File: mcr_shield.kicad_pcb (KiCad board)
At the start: 2 copper layers, 120 x 100 mm, 15 parts, among them J2 MCR_P1_Controls, J3 MCR_System_Coin, J4 MCR_Opt_X_Dial, J5 MCR_P2_Controls, SW1 Game_Selector, SW2 Cabinet_Options, U1 Buck_Regulator, U2 Optocoupler_P1, U3 Optocoupler_Sys, U4 Sync_Buffer, U5 Audio_Amplifier

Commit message: Add and route R2R DAC resistors (R1-R9) to KiCad PCB file
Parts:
- added R1: 3.9k_Red_LSB, R_Axial_DIN0207_L6.3mm_D2.5mm_P7.62mm_Horizontal, F.Cu at (40.0, 30.0)
- added R2: 2.0k_Red_Mid, R_Axial_DIN0207_L6.3mm_D2.5mm_P7.62mm_Horizontal, F.Cu at (40.0, 33.0)
- added R3: 1.0k_Red_MSB, R_Axial_DIN0207_L6.3mm_D2.5mm_P7.62mm_Horizontal, F.Cu at (40.0, 36.0)
- added R4: 3.9k_Green_LSB, R_Axial_DIN0207_L6.3mm_D2.5mm_P7.62mm_Horizontal, F.Cu at (50.0, 30.0)
- added R5: 2.0k_Green_Mid, R_Axial_DIN0207_L6.3mm_D2.5mm_P7.62mm_Horizontal, F.Cu at (50.0, 33.0)
- added R6: 1.0k_Green_MSB, R_Axial_DIN0207_L6.3mm_D2.5mm_P7.62mm_Horizontal, F.Cu at (50.0, 36.0)
- added R7: 3.9k_Blue_LSB, R_Axial_DIN0207_L6.3mm_D2.5mm_P7.62mm_Horizontal, F.Cu at (60.0, 30.0)
- added R8: 2.0k_Blue_Mid, R_Axial_DIN0207_L6.3mm_D2.5mm_P7.62mm_Horizontal, F.Cu at (60.0, 33.0)
- added R9: 1.0k_Blue_MSB, R_Axial_DIN0207_L6.3mm_D2.5mm_P7.62mm_Horizontal, F.Cu at (60.0, 36.0)
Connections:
- JP1 pad 10: (no net) -> FPGA_R1
- JP1 pad 11: (no net) -> FPGA_R2
- JP1 pad 12: CAB_G0 -> FPGA_G0
- JP1 pad 13: (no net) -> FPGA_G1
- JP1 pad 14: (no net) -> FPGA_G2
- JP1 pad 15: CAB_B0 -> FPGA_B0
- JP1 pad 16: (no net) -> FPGA_B1
- JP1 pad 17: (no net) -> FPGA_B2
- JP1 pad 9: CAB_R0 -> FPGA_R0
- J_VID pad 1: CAB_R0 -> CAB_RED
- J_VID pad 3: CAB_G0 -> CAB_GREEN
- J_VID pad 5: CAB_B0 -> CAB_BLUE

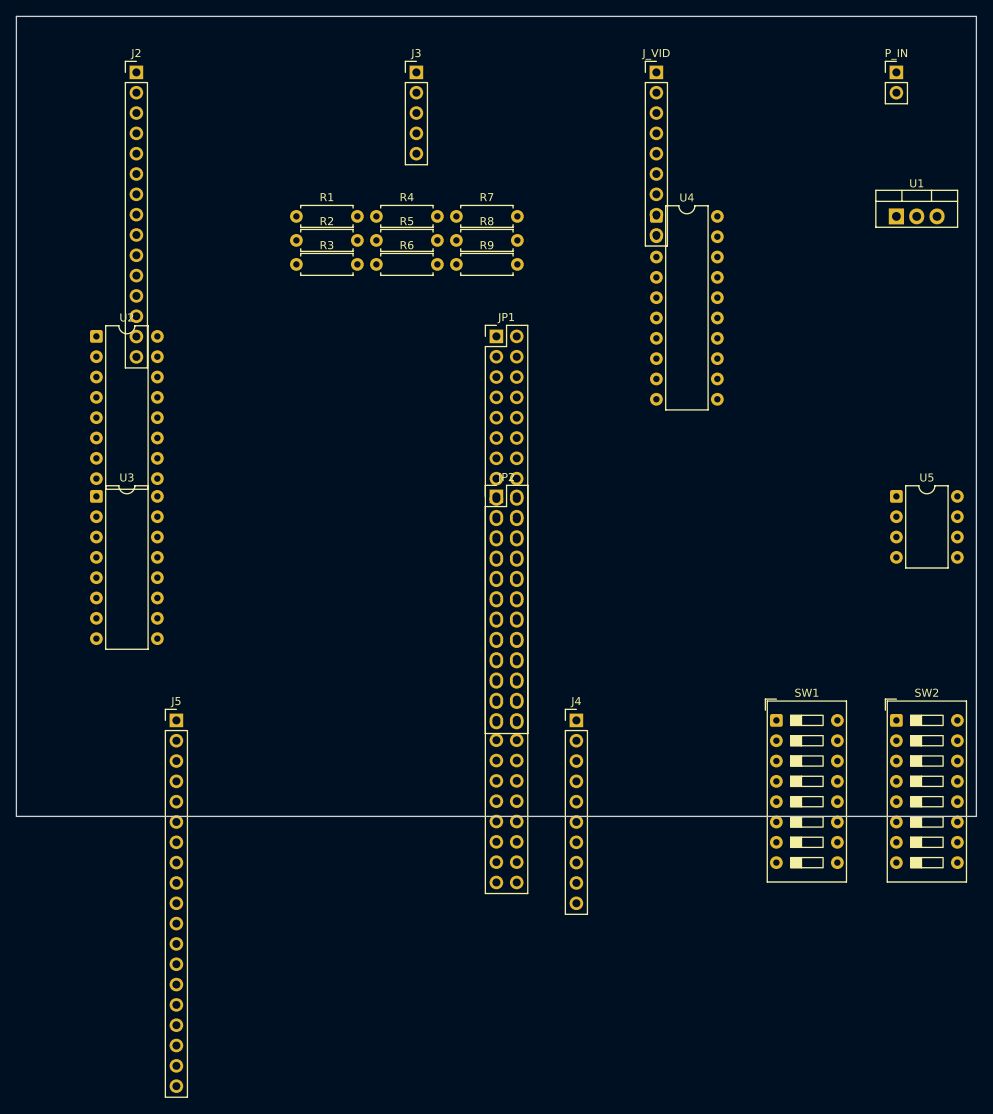
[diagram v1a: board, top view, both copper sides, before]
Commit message: Optimize layout to compact 95mm x 85mm and rotate DIP switches vertically
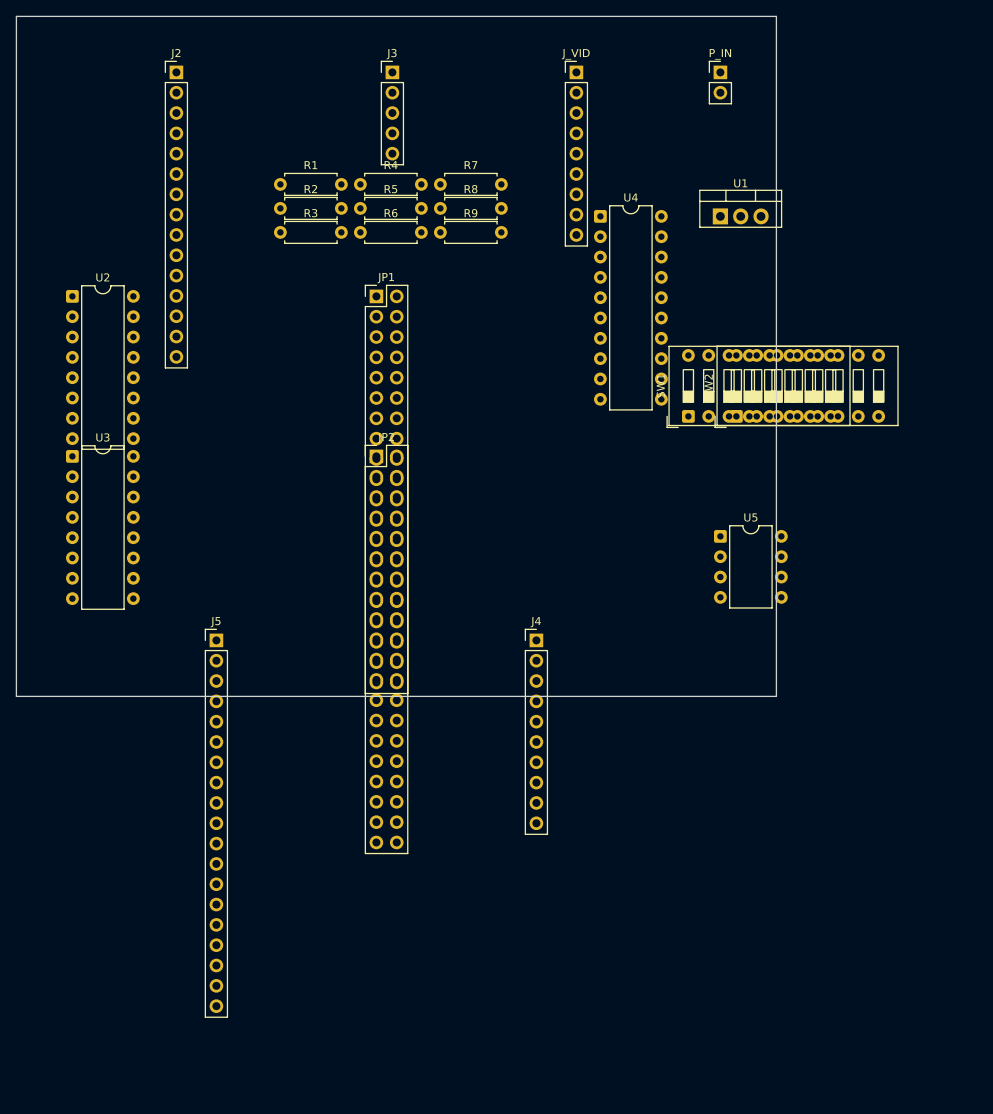
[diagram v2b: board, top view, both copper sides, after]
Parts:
- moved SW2 42.9 mm to (95.0, 55.0), turned to 90 degrees
- moved SW1 39.6 mm to (89.0, 55.0), turned to 90 degrees
- moved U5 22.6 mm to (93.0, 70.0)
- moved P_IN 22.0 mm to (93.0, 12.0)
- moved U1 22.0 mm to (93.0, 30.0)
- moved JP1 15.8 mm to (50.0, 40.0)
- moved JP2 15.8 mm to (50.0, 60.0)
- moved J4 11.2 mm to (70.0, 83.0)
- moved J5 11.2 mm to (30.0, 83.0)
- moved J_VID 10.0 mm to (75.0, 12.0)
- moved U4 7.00 mm to (78.0, 30.0)
- moved U2 5.83 mm to (12.0, 40.0)
- moved U3 5.83 mm to (12.0, 60.0)
- moved J2 5.00 mm to (25.0, 12.0)
- moved R1 4.47 mm to (38.0, 26.0)
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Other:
- board size 120 x 100 mm -> 95 x 85 mm
